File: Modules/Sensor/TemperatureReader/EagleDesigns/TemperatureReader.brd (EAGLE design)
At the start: 100 x 80 mm, 6 parts, among them U1 TINY85-20-DIP, U2 MLX90614_

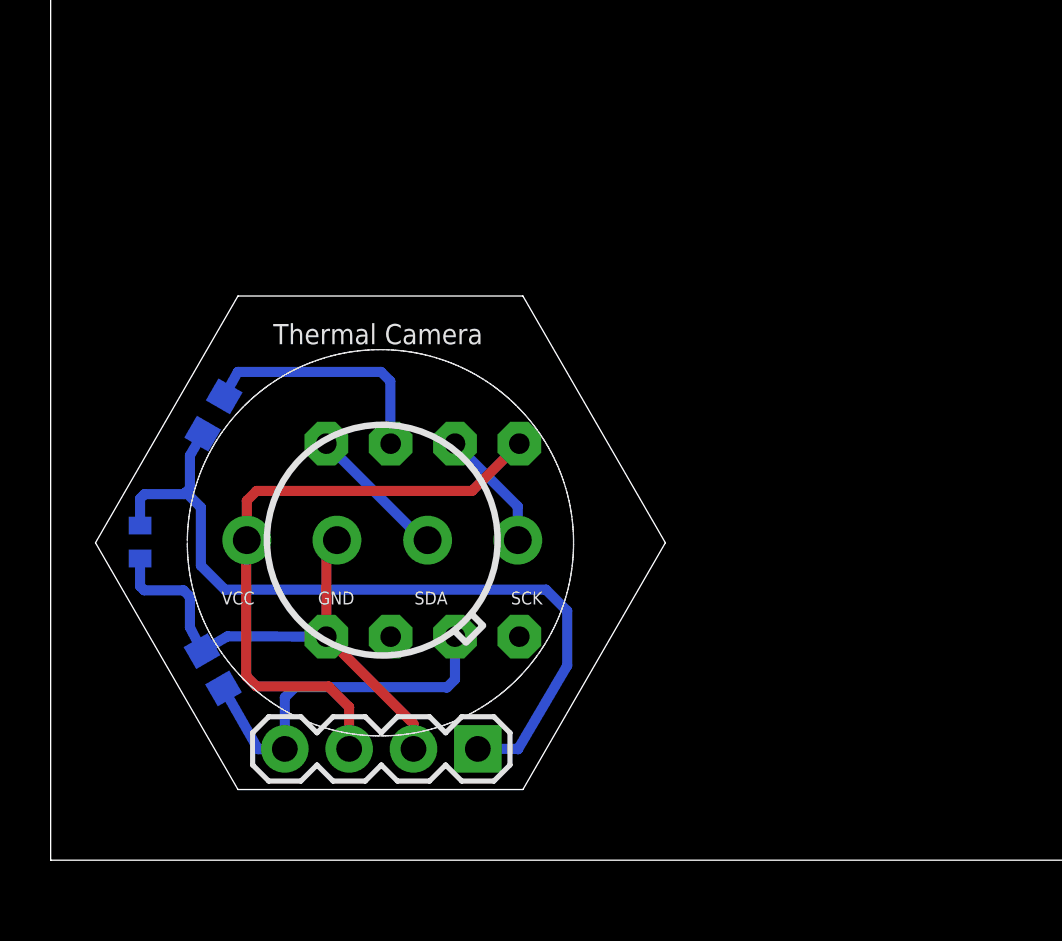
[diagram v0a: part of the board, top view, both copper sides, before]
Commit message: added eagle files for #31
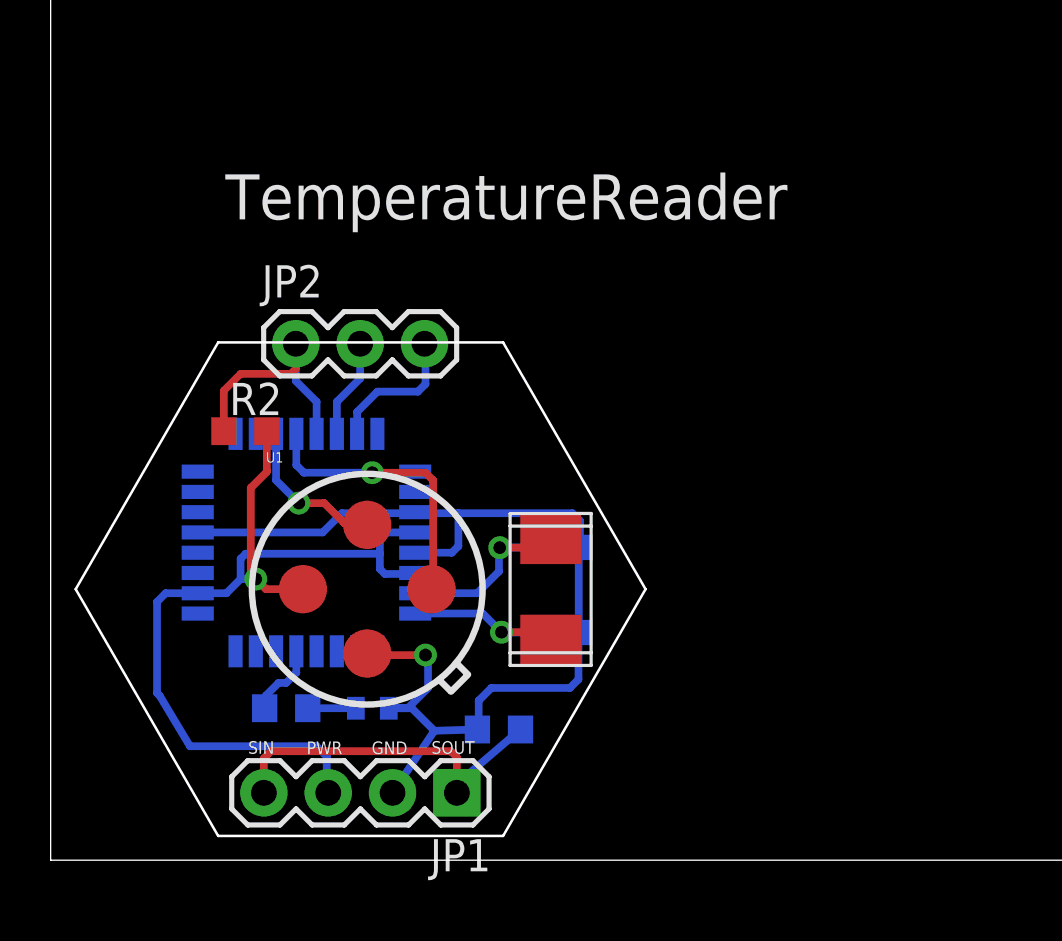
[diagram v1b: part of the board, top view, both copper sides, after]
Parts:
- added C2: 22pF, adafruit:C0603
- added C3: 0.22uF, adafruit:C0402
- added JP2: (no value), SparkFun-Connectors:1X03
- added R4: 4.7K, adafruit:R0603
- added U$2: NX503, MakerWear:NX503
- C1: value 0.22uF -> 22pF; device adafruit:C0402 -> adafruit:C0603
- R2: value 4.7K -> 10K; device adafruit:R0603 -> resistor:R0603
- U1: value TINY85-20-DIP -> MLX90614; device SparkFun-DigitalIC:DIP08 -> MakerWear:TO-39
- U2: value MLX90614_ -> ATMEGA328P_TQFP; device SparkFun-Sensors:TO-39 -> SparkFun-DigitalIC:TQFP32-08
- moved C1 16.5 mm to (20.0, 12.3), turned to 180 degrees
- moved R1 11.5 mm to (17.7, 5.16), turned to 180 degrees
- moved U2 3.00 mm to (10.1, 12.5), flipped to the bottom
- moved U1 2.93 mm to (12.5, 10.7), flipped to the top
- moved JP1 1.92 mm to (16.0, 2.66)
- moved R2 1.42 mm to (7.69, 16.9), flipped to the top, turned to 0 degrees
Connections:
- removed net NRES: U1.1
- removed net OUT(MISO): R2.2, U1.6
- removed net SCK: U1.7, U2.1
- removed net SDA(MOSI): U1.5, U2.2
- new net 1X3SIN-SOUT: JP1.1, JP1.4, R1.2
- new net N$1: C1.1, U$2.P$1, U2.7
- new net N$3: C2.1, U$2.P$2, U2.8
- new net OUT: R4.2, U2.13
- new net RESET: JP2.1, R2.1, U2.29
- new net RX: JP2.2, U2.30
- new net SCL: U1.SCL, U2.28
- new net SDA: U1.PWM, U2.27
- new net TX: JP2.3, U2.31
- net 1X3SIN: now also U2.23; no longer JP1.4, R1.2, U1.2
- net 1X3SOUT: now also C3.1, R4.1; no longer C1.2, JP1.1, R2.1
- net GND: now also C1.2, C2.2, C3.2, U1.VSS, U2.21, U2.3, U2.5; no longer C1.1, U1.4, U2.4
- net VCC: now also R2.2, U1.VDD, U2.18, U2.4, U2.6; no longer U1.8, U2.3
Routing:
- net 1X3SOUT: track 31.4 -> 1.90 mm
- net GND: track 20.4 -> 42.8 mm, vias 0 -> 1
- net 1X3SIN: track 14.6 -> 0.00 mm
- net 1X3SIN-SOUT: track 0.00 -> 14.4 mm
- net VCC: track 24.9 -> 36.2 mm, vias 0 -> 1
- net SCL: track 0.00 -> 11.2 mm, vias 0 -> 1
- net OUT(MISO): track 9.75 -> 0.00 mm
- net RESET: track 0.00 -> 9.68 mm
- net N$1: track 0.00 -> 8.20 mm, vias 0 -> 1
- net N$3: track 0.00 -> 7.13 mm, vias 0 -> 1
- net SDA: track 0.00 -> 6.16 mm, vias 0 -> 1
- net TX: track 0.00 -> 5.62 mm
- net SDA(MOSI): track 5.58 -> 0.00 mm
- net SCK: track 4.84 -> 0.00 mm
- net RX: track 0.00 -> 3.94 mm
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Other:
- outline, holes or cut-outs redrawn
- board text added: "GND"
- board text added: "PWR"
- board text added: "SIN"
- board text added: "SOUT"
- board text added: "TemperatureReader"
- board text removed: "MW-V3"
- board text removed: "Thermal Camera"

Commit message: fixed eagle files for new modules
SIN/SOUT was not correctly connected in them.
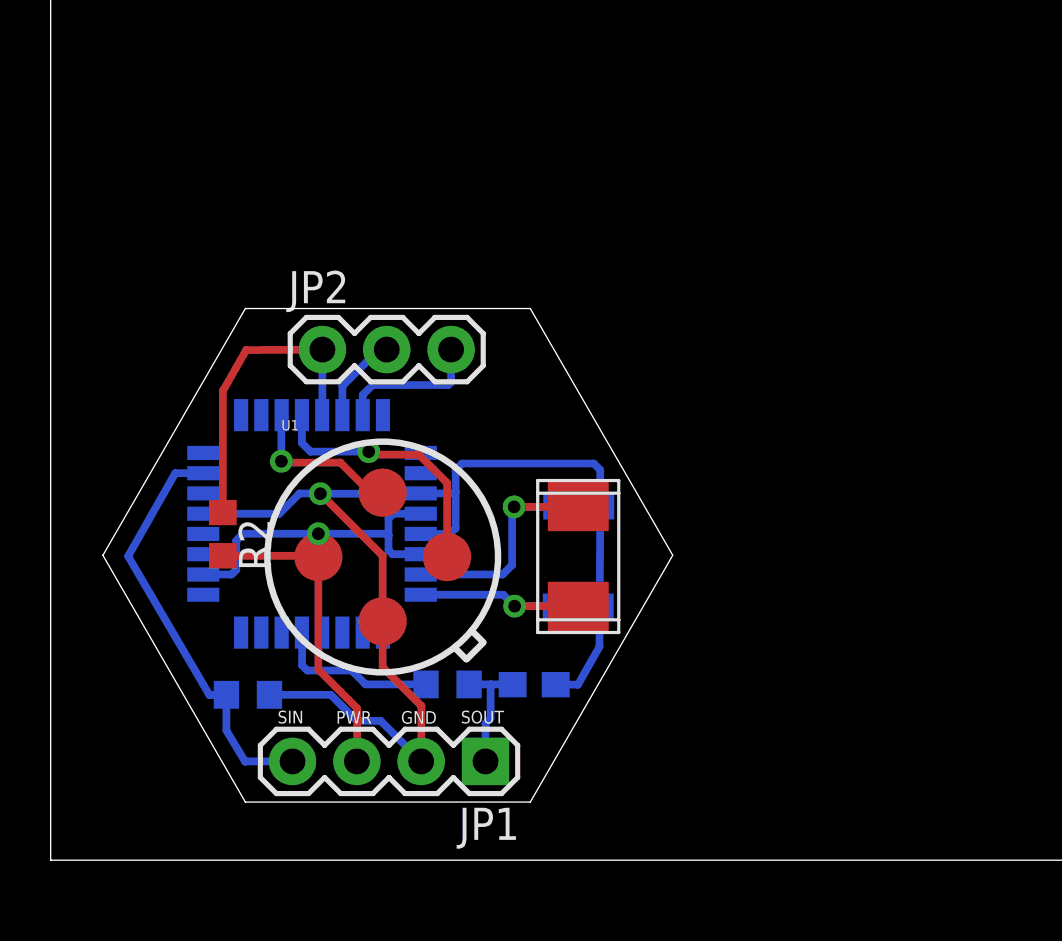
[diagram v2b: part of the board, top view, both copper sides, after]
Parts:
- C3: device adafruit:C0402 -> adafruit:C0603
- moved R1 10.0 mm to (7.79, 6.53), turned to 0 degrees
- moved C3 6.46 mm to (19.1, 6.93)
- moved R4 6.44 mm to (15.7, 6.94)
- moved R2 4.17 mm to (6.80, 12.9), turned to 270 degrees
- moved C1 1.81 mm to (20.9, 13.9)
- moved U$2 1.70 mm to (20.8, 12.0)
- moved JP1 1.68 mm to (17.2, 3.90)
- moved U1 1.41 mm to (13.1, 12.0)
- moved C2 1.34 mm to (20.8, 10.0)
- moved JP2 1.07 mm to (10.7, 20.2)
- moved U2 0.77 mm to (10.3, 13.3)
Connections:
- removed net 1X3SIN-SOUT: JP1.1, JP1.4, R1.2
- net 1X3SIN: now also JP1.4, R1.2
- net 1X3SOUT: now also JP1.1
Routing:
- net 1X3SIN: track 0.00 -> 16.6 mm
- net 1X3SIN-SOUT: track 14.4 -> 0.00 mm
- net VCC: track 36.2 -> 26.1 mm
- net GND: track 42.8 -> 48.9 mm
- net OUT: track 2.94 -> 6.50 mm
- net 1X3SOUT: track 1.90 -> 4.86 mm
- net RESET: track 9.68 -> 12.3 mm
- net N$1: track 8.20 -> 10.3 mm
- net N$3: track 7.13 -> 8.08 mm
- net SCL: track 11.2 -> 10.4 mm
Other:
- outline, holes or cut-outs redrawn
- board text removed: "TemperatureReader"
